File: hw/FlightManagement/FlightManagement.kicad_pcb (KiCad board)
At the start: 2 copper layers, 84 parts, among them J1 BWSMA-KE-Z001, J4 430450412, U12 TPS54202DDC, U2 STM32L431RCTx, U3 MPU-6050, U4 LIS2MDL, U6 XA17-G4K, U8 SN65HVD230, Y1 13.56 MHz, Y2 10.7 MHz

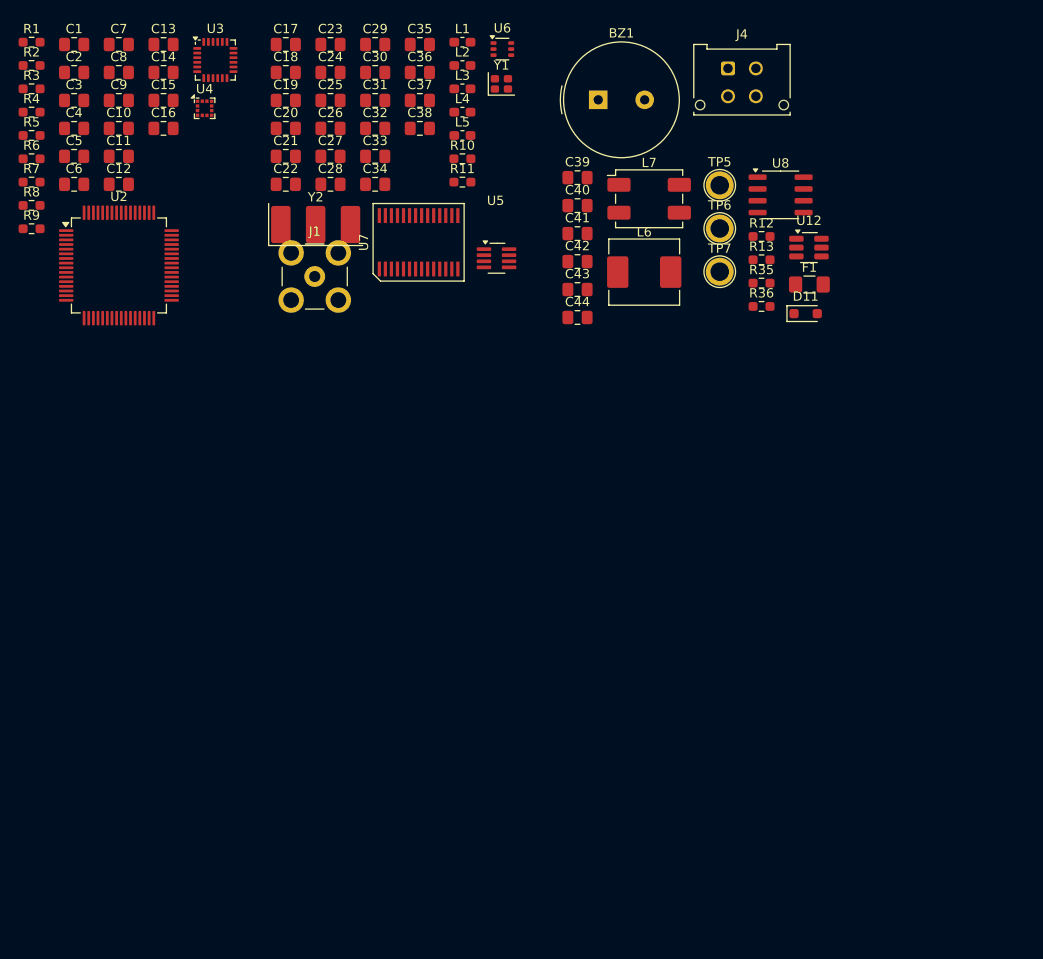
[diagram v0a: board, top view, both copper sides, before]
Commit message: add NOR flash in FC
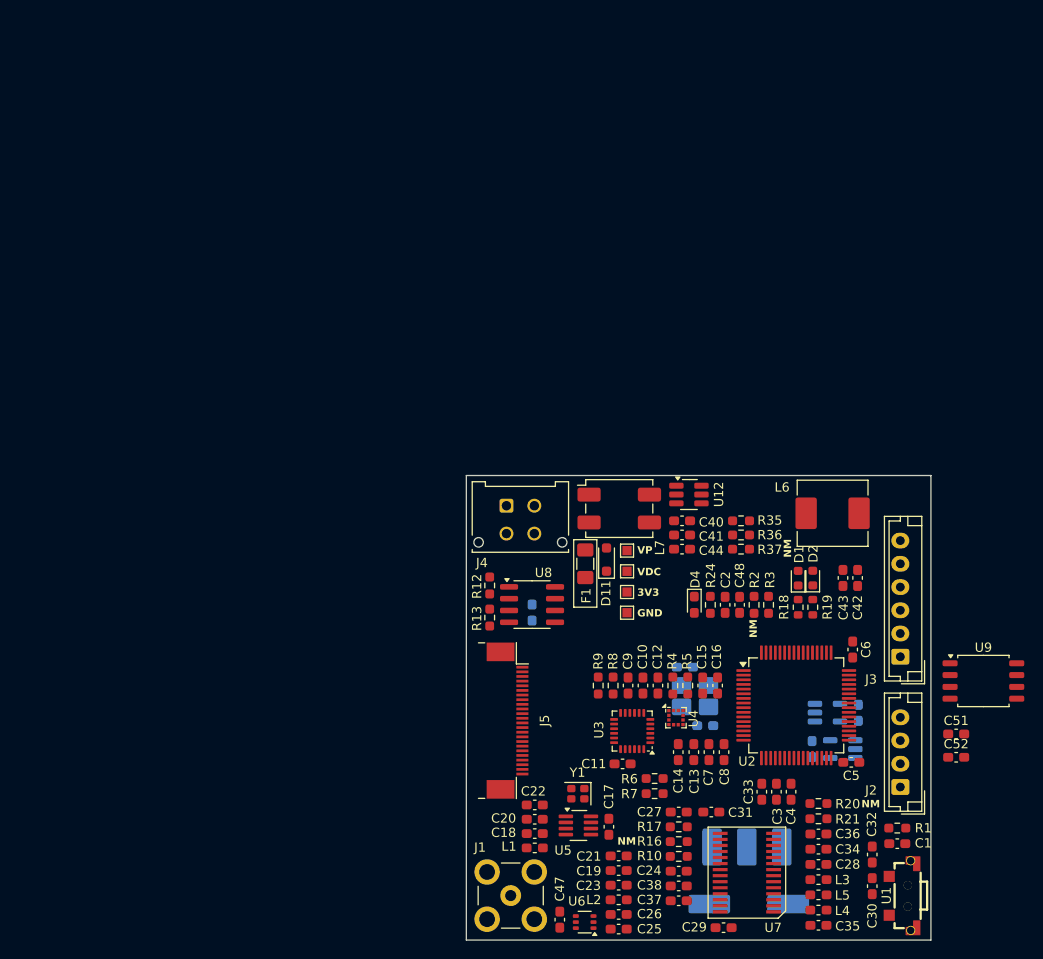
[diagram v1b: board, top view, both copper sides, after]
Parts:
- removed BZ1: Buzzer, Buzzer_Beeper:Buzzer_TDK_PS1240P02BT_D12.2mm_H6.5mm
- removed R11: 0R, Resistor_SMD:R_0603_1608Metric_Pad0.98x0.95mm_HandSolder
- added C45: 10 pF, Capacitor_SMD:C_0603_1608Metric_Pad1.08x0.95mm_HandSolder, B.Cu at (135.8, 98.1)
- added C46: 10 pF, Capacitor_SMD:C_0603_1608Metric_Pad1.08x0.95mm_HandSolder, B.Cu at (138.0, 104.4)
- added C47: 1000 pF, Capacitor_SMD:C_0603_1608Metric_Pad1.08x0.95mm_HandSolder, F.Cu at (122.4, 125.3)
- added C48: 0.1 µF, Capacitor_SMD:C_0603_1608Metric_Pad1.08x0.95mm_HandSolder, F.Cu at (141.7, 91.4)
- added C49: 0.1 µF, Capacitor_SMD:C_0603_1608Metric_Pad1.08x0.95mm_HandSolder, B.Cu at (149.5, 106.9)
- added C50: 0.1 µF, Capacitor_SMD:C_0603_1608Metric_Pad1.08x0.95mm_HandSolder, B.Cu at (154.5, 103.0)
- added C51: 0.1 µF, Capacitor_SMD:C_0603_1608Metric_Pad1.08x0.95mm_HandSolder, F.Cu at (165.0, 105.3)
- added C52: 1 µF, Capacitor_SMD:C_0603_1608Metric_Pad1.08x0.95mm_HandSolder, F.Cu at (165.0, 107.8)
- added D1: RED, LED_SMD:LED_0603_1608Metric, F.Cu at (148.0, 88.5)
- added D2: GREEN, LED_SMD:LED_0603_1608Metric, F.Cu at (149.6, 88.5)
- added D4: KT-0603W, LED_SMD:LED_0603_1608Metric_Pad1.05x0.95mm_HandSolder, F.Cu at (136.8, 91.4)
- added J2: B4B-EH-A(LF)(SN), Connector_JST:JST_EH_B4B-EH-A_1x04_P2.50mm_Vertical, F.Cu at (159.0, 111.0)
- added J3: B6B-EH-A(LF)(SN), Connector_JST:JST_EH_B6B-EH-A_1x06_P2.50mm_Vertical, F.Cu at (159.0, 97.0)
- added J5: Conn_01x24_MountingPin, Connector_FFC-FPC:Jushuo_AFC07-S24FCA-00_1x24-1MP_P0.50_Horizontal, F.Cu at (116.7, 103.9)
- added R16: 0R, Resistor_SMD:R_0603_1608Metric_Pad0.98x0.95mm_HandSolder, F.Cu at (135.2, 116.9)
- added R17: 0R, Resistor_SMD:R_0603_1608Metric_Pad0.98x0.95mm_HandSolder, F.Cu at (135.2, 115.3)
- added R18: 100, Resistor_SMD:R_0603_1608Metric, F.Cu at (148.0, 91.6)
- added R19: 100, Resistor_SMD:R_0603_1608Metric, F.Cu at (149.6, 91.6)
- added R20: 0R, Resistor_SMD:R_0603_1608Metric_Pad0.98x0.95mm_HandSolder, F.Cu at (150.2, 112.8)
- added R21: 0R, Resistor_SMD:R_0603_1608Metric_Pad0.98x0.95mm_HandSolder, F.Cu at (150.2, 114.4)
- added R24: 1 kOhm, Resistor_SMD:R_0603_1608Metric_Pad0.98x0.95mm_HandSolder, F.Cu at (138.6, 91.4)
- added R37: 0 ohm, Resistor_SMD:R_0603_1608Metric_Pad0.98x0.95mm_HandSolder, F.Cu at (141.9, 85.4)
- added TP1: TestPoint_Flag, TestPoint:TestPoint_Pad_1.0x1.0mm, F.Cu at (129.6, 92.2)
- added U1: YTS1C0033BBG01, easyeda2kicad:SW-SMD_YIYUAN_YTS1C003XXX, F.Cu at (159.1, 122.7)
- added U14: SN74LVC1G125DBV, Package_TO_SOT_SMD:SOT-23-5_HandSoldering, B.Cu at (152.8, 106.9)
- added U15: SN74LVC1G125DBV, Package_TO_SOT_SMD:SOT-23-5_HandSoldering, B.Cu at (151.2, 103.0)
- added U9: W25Q128JVS, Package_SO:SOIC-8_5.3x5.3mm_P1.27mm, F.Cu at (167.9, 99.6)
- added Y3: 6.6128 MHz, Crystal:Crystal_SMD_HC49-SD, B.Cu at (142.7, 123.6)
- added Y4: Crystal_GND24, Crystal:Crystal_SMD_3225-4Pin_3.2x2.5mm_HandSoldering, B.Cu at (136.9, 101.2)
- C1, C10, C11, C12, C13, C14, C15, C16, C17, C18, C19, C2, C20, C21, C22, C23, C24, C25, C26, C27, C28, C29, C3, C30, C31, C32, C33, C34, C35, C36, C37, C38, C4, C40, C41, C42, C43, C44, C5, C6, C7, C8, C9: footprint Capacitor_SMD:C_0805_2012Metric_Pad1.18x1.45mm_HandSolder -> Capacitor_SMD:C_0603_1608Metric_Pad1.08x0.95mm_HandSolder
- C39: footprint Capacitor_SMD:C_0805_2012Metric_Pad1.18x1.45mm_HandSolder -> Capacitor_SMD:C_0603_1608Metric_Pad1.08x0.95mm_HandSolder; moved to B.Cu
- TP5, TP6, TP7: footprint TestPoint:TestPoint_Plated_Hole_D2.0mm -> TestPoint:TestPoint_Pad_1.0x1.0mm
- Y2: moved to B.Cu
- moved R1 125.8 mm to (158.7, 115.4), turned to 180 degrees
- moved C1 123.5 mm to (158.7, 117.1)
- moved C5 106.1 mm to (153.7, 108.3), turned to 180 degrees
- moved C3 106.1 mm to (145.7, 111.5), turned to -90 degrees
- moved C4 105.1 mm to (147.2, 111.5), turned to 90 degrees
- moved C35 104.1 mm to (150.2, 125.9), turned to 180 degrees
- moved C30 102.6 mm to (156.0, 121.7), turned to -90 degrees
- moved C29 102.2 mm to (140.0, 126.1), turned to 180 degrees
- moved C7 99.2 mm to (138.4, 107.2), turned to 90 degrees
- moved C8 97.9 mm to (140.0, 107.2), turned to 90 degrees
- moved C6 97.6 mm to (153.9, 96.2), turned to -90 degrees
- moved R2 97.0 mm to (143.3, 91.4), turned to -90 degrees
- moved R3 96.8 mm to (144.8, 91.4), turned to 90 degrees
- moved C23 95.7 mm to (128.7, 121.6), turned to 180 degrees
- moved C13 95.2 mm to (136.8, 107.2), turned to -90 degrees
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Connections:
- R2 pad 2: Net-(R2-Pad2) -> Net-(U2-PH3)
- R3 pad 1: Net-(R2-Pad2) -> Net-(U2-PH3)
- U2 pad 10: unconnected-(U2-PC2-Pad10) -> /AGCDIS
- U2 pad 12: unconnected-(U2-VSSA-Pad12) -> GND
- U2 pad 13: unconnected-(U2-VDDA-Pad13) -> +3V3
- U2 pad 15: unconnected-(U2-PA1-Pad15) -> /MAG_INT
- U2 pad 16: unconnected-(U2-PA2-Pad16) -> /TXCLK
- U2 pad 17: unconnected-(U2-PA3-Pad17) -> /FSYNC
- U2 pad 18: Net-(U2-VSS-Pad18) -> GND
- U2 pad 22: unconnected-(U2-PA6-Pad22) -> /TXDATA
- U2 pad 23: unconnected-(U2-PA7-Pad23) -> /NCS_NOR
- U2 pad 24: unconnected-(U2-PC4-Pad24) -> Net-(U2-PC4)
- U2 pad 25: unconnected-(U2-PC5-Pad25) -> Net-(U2-PC5)
- U2 pad 26: unconnected-(U2-PB0-Pad26) -> /RXEN
- U2 pad 27: unconnected-(U2-PB1-Pad27) -> /TXEN
- U2 pad 28: unconnected-(U2-PB2-Pad28) -> /PDOUT
- U2 pad 3: unconnected-(U2-PC14-Pad3) -> Net-(D2-A)
- U2 pad 31: Net-(U2-VSS-Pad18) -> GND
- U2 pad 4: unconnected-(U2-PC15-Pad4) -> Net-(D1-A)
- U2 pad 46: /MAG_INT -> /SWDIO
- U2 pad 47: Net-(U2-VSS-Pad18) -> GND
- U2 pad 49: Net-(U2-PA14) -> /SWCLK
- U2 pad 5: unconnected-(U2-PH0-Pad5) -> Net-(U2-PH0)
- U2 pad 55: unconnected-(U2-PB3-Pad55) -> Net-(U2-PB3)
- U2 pad 56: unconnected-(U2-PB4-Pad56) -> Net-(U2-PB4)
- U2 pad 57: unconnected-(U2-PB5-Pad57) -> Net-(U2-PB5)
- U2 pad 58: unconnected-(U2-PB6-Pad58) -> Net-(U2-PB6)
- U2 pad 59: unconnected-(U2-PB7-Pad59) -> Net-(U2-PB7)
- U2 pad 6: unconnected-(U2-PH1-Pad6) -> Net-(U2-PH1)
- U2 pad 60: unconnected-(U2-PH3-Pad60) -> Net-(U2-PH3)
- U2 pad 63: Net-(U2-VSS-Pad18) -> GND
- U2 pad 8: unconnected-(U2-PC0-Pad8) -> /DATAOUT
- U2 pad 9: unconnected-(U2-PC1-Pad9) -> +3V3
- U3 pad 11: Net-(U2-PA14) -> /FSYNC
- U5 pad 5: unconnected-(U5-CLKOUT-Pad5) -> /TXCLK
- U5 pad 6: unconnected-(U5-DATA-Pad6) -> /TXDATA
- U6 pad 4: unconnected-(U6-V2-Pad4) -> /TXEN
- U6 pad 5: Net-(J1-In) -> Net-(U6-RFC)
- U6 pad 6: unconnected-(U6-V1-Pad6) -> /RXEN
- U7 pad 1: unconnected-(U7-XTAL1-Pad1) -> Net-(U7-XTAL1)
- U7 pad 11: +3V3 -> Net-(U7-IRSEL)
- U7 pad 15: /RF/AGCDIS -> /AGCDIS
- U7 pad 16: unconnected-(U7-XTALSEL-Pad16) -> Net-(U7-XTALSEL)
- U7 pad 25: /RF/DATAOUT -> /DATAOUT
- U7 pad 26: unconnected-(U7-PDOUT-Pad26) -> /PDOUT
- U7 pad 27: Net-(U7-PWRDN) -> +3V3
- U7 pad 28: unconnected-(U7-XTAL2-Pad28) -> Net-(U7-XTAL2)
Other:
- board outline added: 50 x 50 mm
- board text added: "3V3"
- board text added: "GND"
- board text added: "NM"
- board text added: "VDC"
- board text added: "VP"

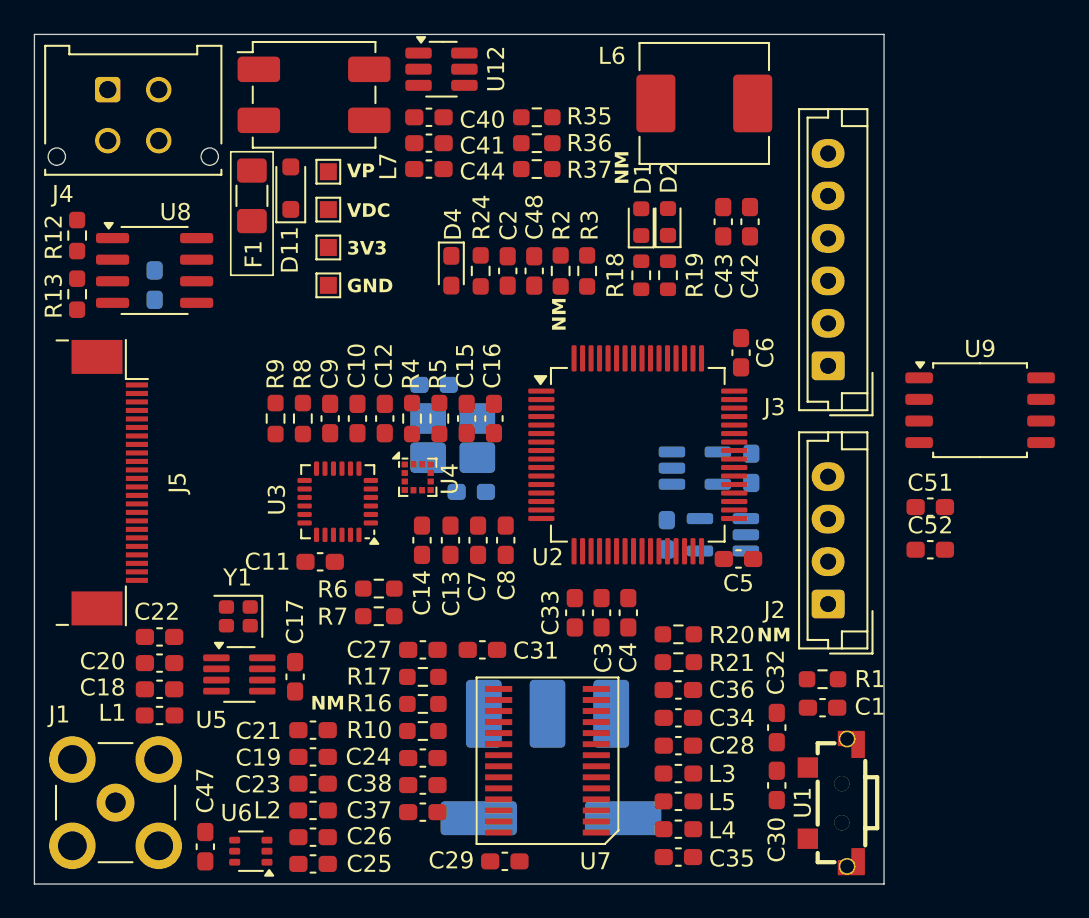
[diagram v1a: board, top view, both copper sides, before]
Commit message: final FC placement
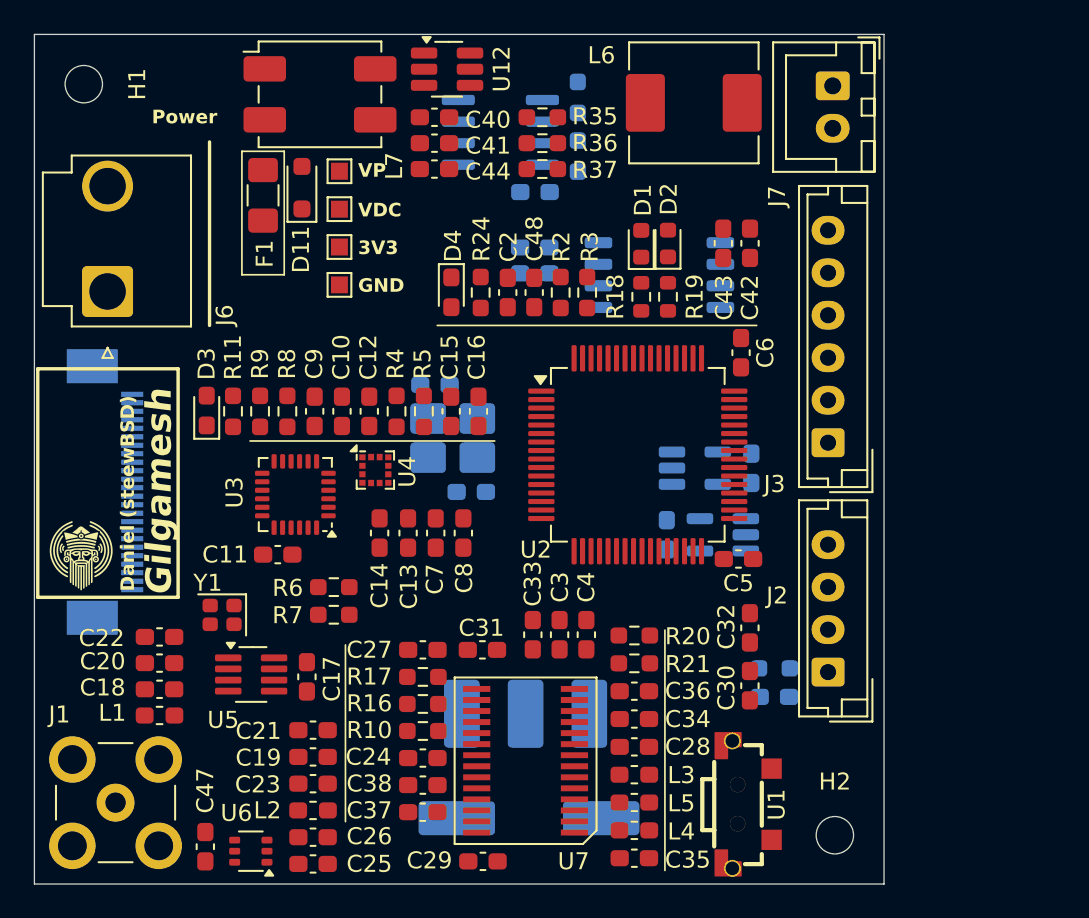
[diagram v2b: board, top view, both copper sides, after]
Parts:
- removed J4: 430450412, Connector_Molex:Molex_Micro-Fit_3.0_43045-0412_2x02_P3.00mm_Vertical
- added D3: KT-0603W, LED_SMD:LED_0603_1608Metric_Pad1.05x0.95mm_HandSolder, F.Cu at (122.4, 99.6)
- added H1: MountingHole, MountingHole:MountingHole_2.2mm_M2, F.Cu at (115.2, 80.4)
- added H2: MountingHole, MountingHole:MountingHole_2.2mm_M2, F.Cu at (159.4, 124.6)
- added J6: Conn_01x02_Socket, steew:JST_VL_B02P-VL_1x02_P6.2mm_Vertical, F.Cu at (116.6, 93.7)
- added J7: Conn_01x02_Pin, Connector_JST:JST_XH_B2B-XH-A_1x02_P2.50mm_Vertical, F.Cu at (159.3, 80.5)
- added R11: 1 kOhm, Resistor_SMD:R_0603_1608Metric_Pad0.98x0.95mm_HandSolder, F.Cu at (124.0, 99.7)
- C1, C51, C52, J5, R1, R12, R13, U8, U9: moved to B.Cu
- moved R12 30.6 mm to (144.3, 81.2)
- moved R13 30.6 mm to (144.3, 84.6)
- moved C52 28.4 mm to (141.7, 91.5)
- moved C51 27.8 mm to (141.7, 90.0)
- moved C39 23.0 mm to (141.8, 86.8), turned to 0 degrees
- moved U8 21.9 mm to (139.7, 83.2), turned to 180 degrees
- moved U9 20.5 mm to (149.1, 91.6), turned to 180 degrees
- moved C30 6.08 mm to (154.4, 115.8)
- moved C32 6.08 mm to (154.4, 112.4)
- moved U1 4.69 mm to (154.4, 122.8), turned to -90 degrees
- moved J3 4.52 mm to (159.0, 101.5)
- moved J2 4.00 mm to (159.0, 115.0)
- moved C1 2.90 mm to (155.8, 116.5), turned to 180 degrees
- moved R1 2.90 mm to (155.8, 114.8), turned to 0 degrees
- moved C3 2.79 mm to (143.2, 112.8)
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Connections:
- J5 pad 1: unconnected-(J5-Pin_1-Pad1) -> GND
- J5 pad 10: unconnected-(J5-Pin_10-Pad10) -> /CAMERA11
- J5 pad 11: unconnected-(J5-Pin_11-Pad11) -> /CAMERA10
- J5 pad 12: unconnected-(J5-Pin_12-Pad12) -> /CAMERA9
- J5 pad 13: unconnected-(J5-Pin_13-Pad13) -> /CAMERA8
- J5 pad 14: unconnected-(J5-Pin_14-Pad14) -> /CAMERA7
- J5 pad 15: unconnected-(J5-Pin_15-Pad15) -> /CAMERA6
- J5 pad 16: unconnected-(J5-Pin_16-Pad16) -> /CAMERA5
- J5 pad 17: unconnected-(J5-Pin_17-Pad17) -> /CAMERA4
- J5 pad 18: unconnected-(J5-Pin_18-Pad18) -> /CAMERA3
- J5 pad 19: unconnected-(J5-Pin_19-Pad19) -> /CAMERA2
- J5 pad 2: unconnected-(J5-Pin_2-Pad2) -> GND
- J5 pad 20: unconnected-(J5-Pin_20-Pad20) -> /CAMERA1
- J5 pad 21: unconnected-(J5-Pin_21-Pad21) -> /CAMERA0
- J5 pad 22: unconnected-(J5-Pin_22-Pad22) -> +3V3
- J5 pad 23: unconnected-(J5-Pin_23-Pad23) -> +3V3
- J5 pad 24: unconnected-(J5-Pin_24-Pad24) -> +3V3
- J5 pad 3: unconnected-(J5-Pin_3-Pad3) -> GND
- J5 pad 5: unconnected-(J5-Pin_5-Pad5) -> GND
- J5 pad 6: unconnected-(J5-Pin_6-Pad6) -> Net-(J5-Pin_6)
- J5 pad 7: unconnected-(J5-Pin_7-Pad7) -> /CAMERA14
- J5 pad 8: unconnected-(J5-Pin_8-Pad8) -> /CAMERA13
- J5 pad 9: unconnected-(J5-Pin_9-Pad9) -> /CAMERA12
- U2 pad 2: unconnected-(U2-PC13-Pad2) -> /CAMERA11
- U2 pad 33: unconnected-(U2-PB12-Pad33) -> /CAMERA3
- U2 pad 34: unconnected-(U2-PB13-Pad34) -> /CAMERA2
- U2 pad 35: unconnected-(U2-PB14-Pad35) -> /CAMERA1
- U2 pad 36: unconnected-(U2-PB15-Pad36) -> /CAMERA0
- U2 pad 37: unconnected-(U2-PC6-Pad37) -> /CAMERA4
- U2 pad 38: unconnected-(U2-PC7-Pad38) -> /CAMERA5
- U2 pad 39: unconnected-(U2-PC8-Pad39) -> /CAMERA6
- U2 pad 40: unconnected-(U2-PC9-Pad40) -> /CAMERA7
- U2 pad 51: unconnected-(U2-PC10-Pad51) -> /CAMERA8
- U2 pad 52: unconnected-(U2-PC11-Pad52) -> /CAMERA9
- U2 pad 53: unconnected-(U2-PC12-Pad53) -> /CAMERA10
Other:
- board text added: "Daniel (steewBSD)"
- board text added: "Gilgamesh"
- board text added: "Power"
- board text removed: "NM"

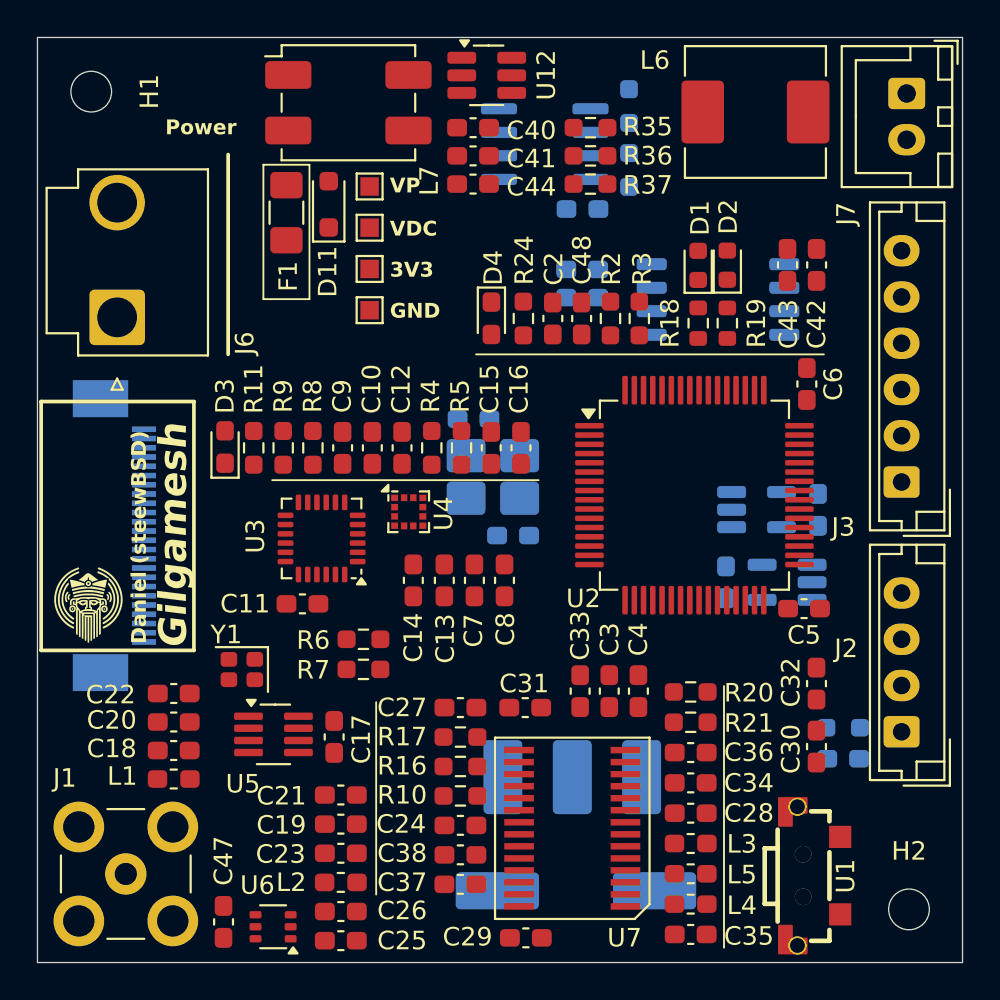
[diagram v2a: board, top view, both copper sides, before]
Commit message: add power monitor
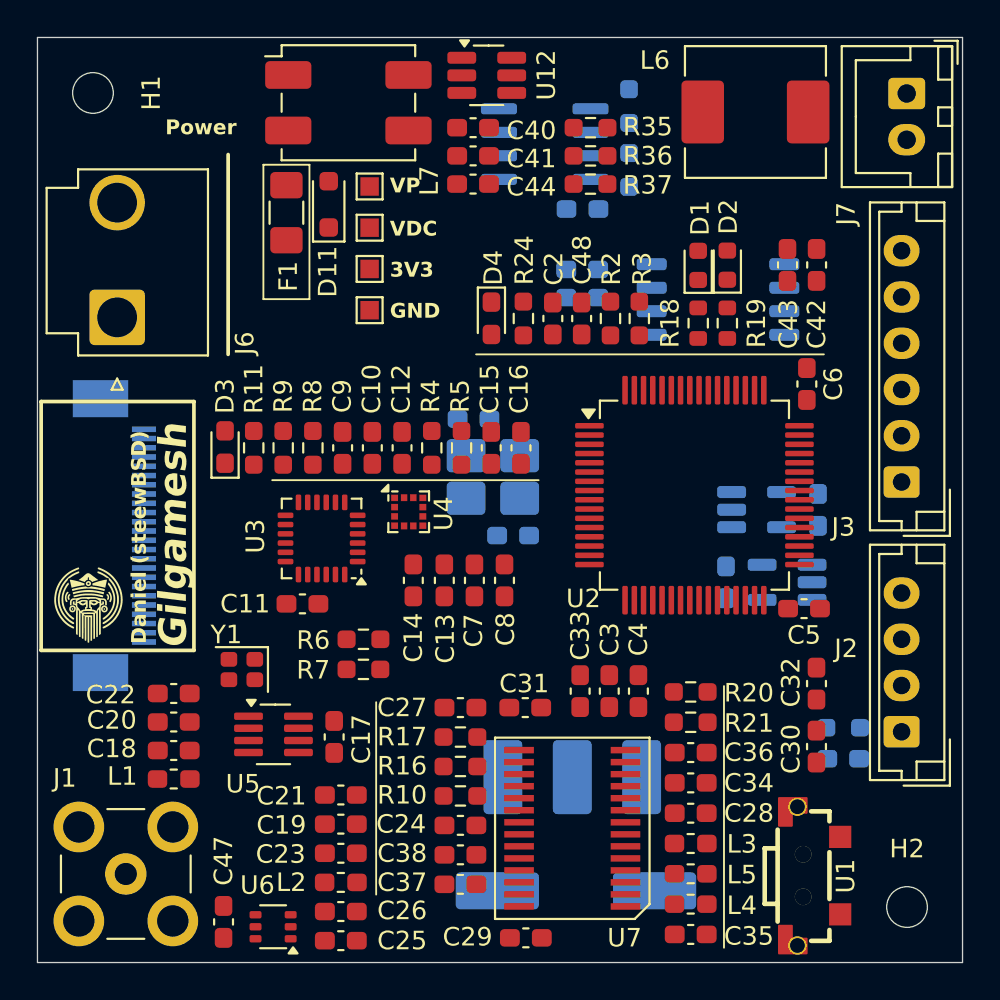
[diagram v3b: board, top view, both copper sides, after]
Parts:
- moved H2 0.17 mm to (159.3, 124.5)
- moved H1 0.12 mm to (115.3, 80.5)
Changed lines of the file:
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@@
 	(footprint "MountingHole:MountingHole_2.2mm_M2"
 		(layer "F.Cu")
-		(at 115.2 80.4 -90)
+		(at 115.2934 80.4719 -90)
 		(descr "Mounting Hole 2.2mm, M2, no annular, generated by kicad-footprint-generator mountinghole.py")
 		(tags "mountinghole M2")
@@
 	(footprint "MountingHole:MountingHole_2.2mm_M2"
 		(layer "F.Cu")
-		(at 159.4 124.6)
+		(at 159.2934 124.4719)
 		(descr "Mounting Hole 2.2mm, M2, no annular, generated by kicad-footprint-generator mountinghole.py")
 		(tags "mountinghole M2")
